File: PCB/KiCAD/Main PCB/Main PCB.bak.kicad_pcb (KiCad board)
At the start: 2 copper layers, 118 x 118 mm, 130 parts, among them IC1 ADG608BRZ, IC2 ADG608BRZ, IC3 VNH7070ASTR, IC4 VNH7070ASTR, IC5 VNH7070ASTR, IC6 VNH7070ASTR, IC7 VNH7070ASTR, IC8 XB3-24Z8CM, J1 Conn_01x04, J10 Conn_01x02, J11 Conn_01x02, J2 Conn_01x04, J3 Conn_01x04, J4 Conn_01x02, J5 Conn_01x02, J6 Conn_01x04_MountingPin, J7 Conn_01x04_MountingPin, J8 Conn_Coaxial_Small, J9 Conn_01x02, M1 Conn_01x02, M2 Conn_01x02, M3 Conn_01x02, M4 Conn_01x02, Q1 BSS138, Q2 BSS138, U1 Teensy4.1, U3 Teensy4.0

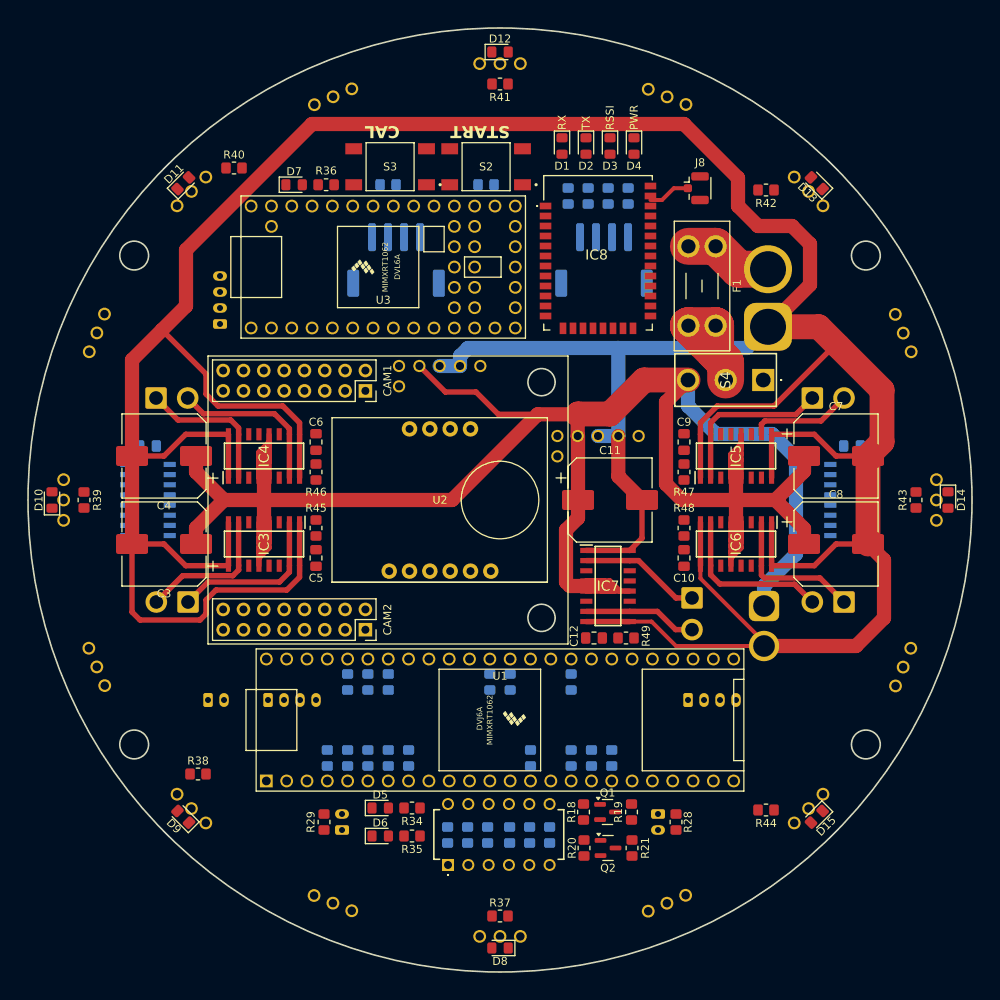
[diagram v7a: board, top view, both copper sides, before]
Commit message: Added another switch
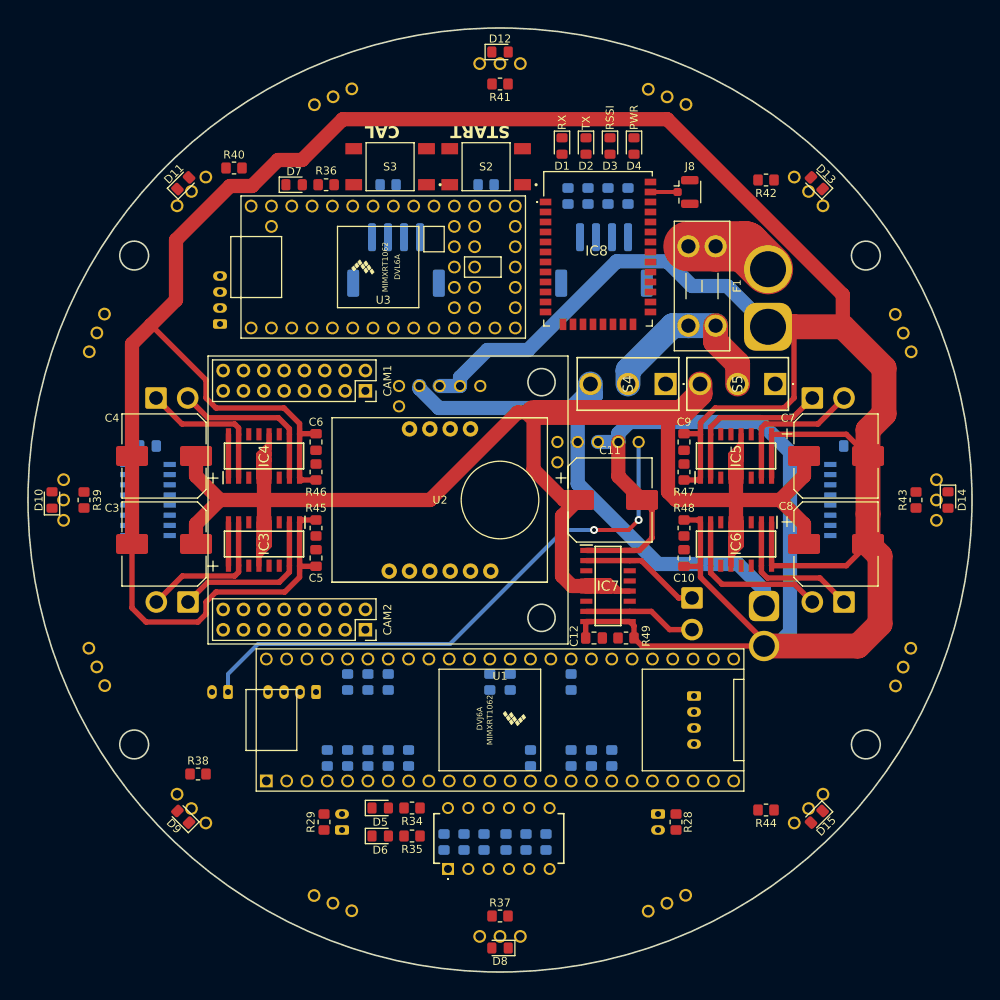
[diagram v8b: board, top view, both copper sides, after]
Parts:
- removed Q1, Q2: BSS138, Package_TO_SOT_SMD:SOT-23
- removed R18, R19, R20, R21: 10k, Resistor_SMD:R_0805_2012Metric_Pad1.20x1.40mm_HandSolder
- added S5: 1101M2S3CGE2, 1101M2S3CGE2:1101M2S3CGE2, F.Cu at (34.4, -14.5)
- IR1, IR10, IR11, IR12, IR13, IR14, IR15, IR16, IR2, IR3, IR4, IR5, IR6, IR7, IR8, IR9: value TSSP4038 -> TSOP34840
- moved S4 12.2 mm to (20.7, -14.5)
- moved J1 6.08 mm to (-23.0, 24.0), turned to 180 degrees
- moved J10 2.69 mm to (-34.0, 24.0), turned to 180 degrees
- moved U5 2.50 mm to (-9.99, -5.12)
- moved J8 1.36 mm to (23.2, -38.5)
- moved R42 1.25 mm to (33.2, -40.0)
- moved R1 0.99 mm to (-7.00, 42.8), turned to -90 degrees
- moved R11 0.99 mm to (3.25, 42.8), turned to -90 degrees
- moved R16 0.99 mm to (5.75, 42.8), turned to -90 degrees
- moved R2 0.99 mm to (-4.50, 42.8), turned to -90 degrees
- moved R10 0.99 mm to (0.75, 42.8), turned to -90 degrees
- moved R5 0.99 mm to (-2.00, 42.8), turned to -90 degrees
- moved J3 0.90 mm to (24.2, 24.5), turned to -90 degrees
- moved U4 0.75 mm to (9.80, 1.88)
- moved IC8 0.50 mm to (12.2, -23.5)
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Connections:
- C11 pad 1: +12V -> +12V_MOTOR
- C3 pad 1: +12V -> +12V_MOTOR
- C4 pad 1: +12V -> +12V_MOTOR
- C7 pad 1: +12V -> +12V_MOTOR
- C8 pad 1: +12V -> +12V_MOTOR
- IC3 pad 12: +12V -> +12V_MOTOR
- IC3 pad 4: +12V -> +12V_MOTOR
- IC3 pad 5: +12V -> +12V_MOTOR
- IC4 pad 12: +12V -> +12V_MOTOR
- IC4 pad 4: +12V -> +12V_MOTOR
- IC4 pad 5: +12V -> +12V_MOTOR
- IC5 pad 12: +12V -> +12V_MOTOR
- IC5 pad 4: +12V -> +12V_MOTOR
- IC5 pad 5: +12V -> +12V_MOTOR
- IC6 pad 12: +12V -> +12V_MOTOR
- IC6 pad 4: +12V -> +12V_MOTOR
- IC6 pad 5: +12V -> +12V_MOTOR
- IC7 pad 12: +12V -> +12V_MOTOR
- IC7 pad 4: +12V -> +12V_MOTOR
- IC7 pad 5: +12V -> +12V_MOTOR
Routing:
- net +12V_MOTOR: track 0.00 -> 286.5 mm
- net +12V: track 329.8 -> 65.0 mm
- net +3V3: track 0.00 -> 71.3 mm, vias 0 -> 2
- net GND: track 503.0 -> 547.1 mm
- net OUT_B_M3: track 12.9 -> 18.1 mm
- net Net-(IC8-RF): track 5.28 -> 3.40 mm
- net Net-(S4-COM): track 22.1 -> 23.4 mm
